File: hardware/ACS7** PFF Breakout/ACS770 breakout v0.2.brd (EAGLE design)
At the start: 54.3 x 21.6 mm, 19 parts

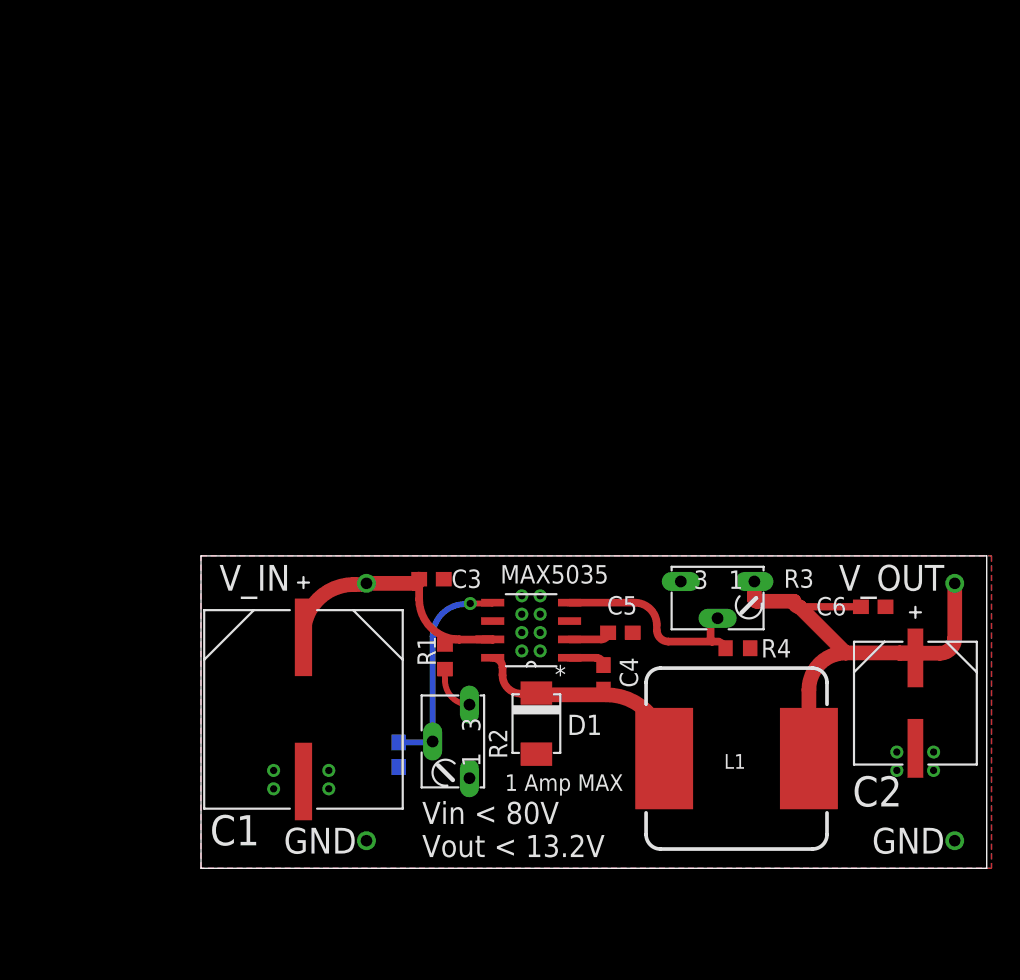
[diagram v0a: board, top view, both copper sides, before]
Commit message: acs7** addition, emonBuck update
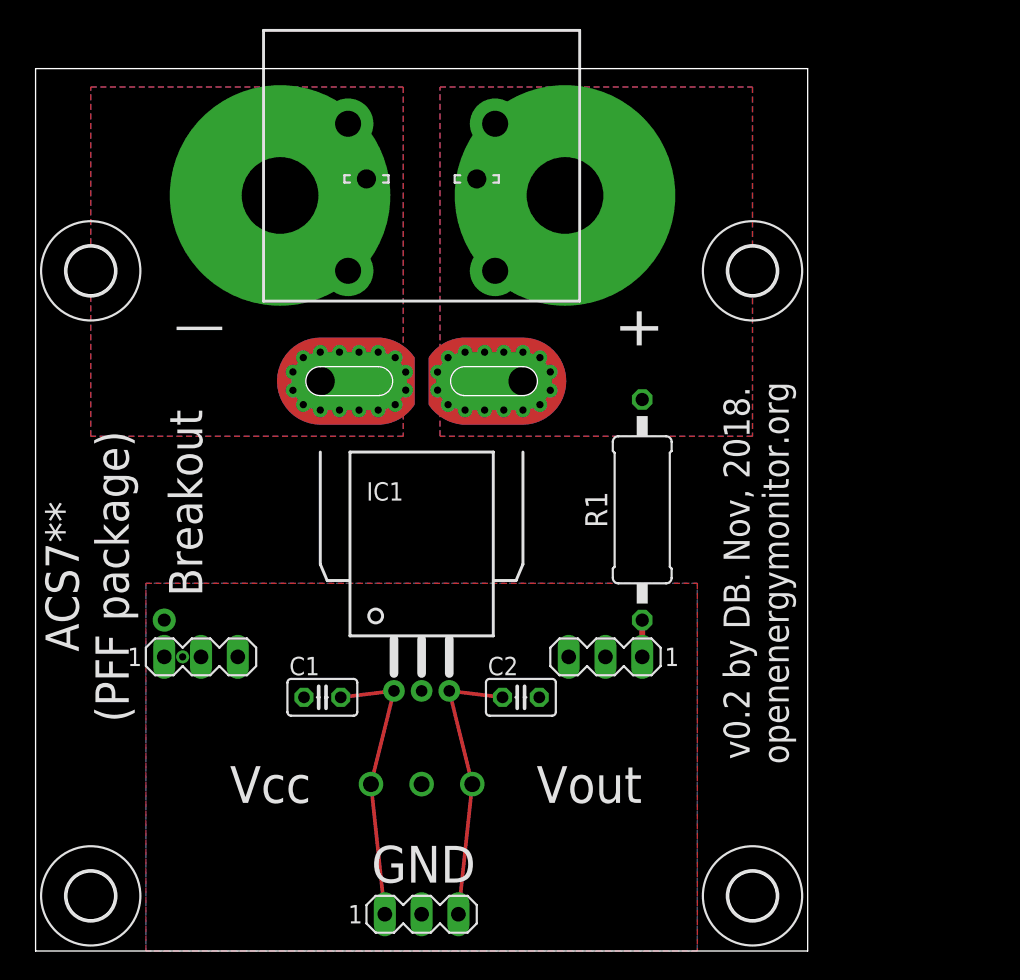
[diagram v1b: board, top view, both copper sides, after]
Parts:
- removed C3, C4, C5, C6, C7: 0.1uF 100V, rcl:C0603
- removed D1: MBRS1100T3G, diodes:SMB_1
- removed L1: SRR1208, inductor-bourns:SSR1208
- removed LOGO1: OSHW_LOGO_6MILX0200-NT, ohw-logo:OSHW_6X200_NOTEXT
- removed MAX5035: MAX5035, MAX5035:21-0111D_SBE-14
- removed R2, R3: 200k, pot:B64W
- removed R4: 10k, rcl@1:R0603
- added IC1: ACS770_PFF, allegro:CB-PFF
- added LSP1, LSP2: LSP13, solpad:LSP13
- added SV1, SV2, SV3: (no value), con-lstb:MA03-1
- added U$5: MOLEX_39970-003, 10.16mm terminal block:2/10,16
- added X1: 1751251, con-phoenix-350:1751251
- C1: value 100uF 80V -> 1nF; device Panasonic-EEE-EEV-EEF-ECQ:CAPAE1350X1400N -> rcl7:C025-025X050
- C2: value 470uF 16V -> 1nF; device Panasonic-EEEFK_EEEFP:CAPAE830X1050N -> rcl7:C025-025X050
- R1: value 700K -> 1M; device rcl@1:R0603 -> rcl:0411/15
- U$1, U$2, U$3, U$4: value TP0.8MM -> (none); device testpad_db:TP0.8 -> holes:3,3
- moved U$4 59.8 mm to (3.81, 3.81)
- moved U$2 47.6 mm to (49.5, 47.0)
- moved U$1 28.8 mm to (3.81, 47.0)
- moved C2 27.3 mm to (33.5, 17.5), turned to 0 degrees
- moved U$3 25.7 mm to (49.5, 3.81)
- moved R1 17.0 mm to (41.9, 30.5), turned to 270 degrees
- moved C1 1.55 mm to (19.8, 17.5), turned to 0 degrees
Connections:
- removed net BST: C4.1, MAX5035.1
- removed net LX: C4.2, D1.C, L1.1, MAX5035.8
- removed net PRE_6.5V: C2.1, C6.1, L1.2, R3.A, U$3.P$1
- removed net VD: C5.1, MAX5035.2
- removed net V_IN_POSTFUSE: C1.1, C3.1, MAX5035.7, R1.2, U$1.P$1
- new net N$4: IC1.IP-, IC1.IP-@10, IC1.IP-@11, IC1.IP-@12, IC1.IP-@13, IC1.IP-@14, IC1.IP-@15, IC1.IP-@16, IC1.IP-@17, IC1.IP-@2, IC1.IP-@3, IC1.IP-@4, IC1.IP-@5, IC1.IP-@6, IC1.IP-@7, IC1.IP-@8, IC1.IP-@9, LSP2.MP, U$5.P$3, U$5.P$4
- new net N$5: IC1.IP+, IC1.IP+@10, IC1.IP+@11, IC1.IP+@12, IC1.IP+@13, IC1.IP+@14, IC1.IP+@15, IC1.IP+@16, IC1.IP+@17, IC1.IP+@2, IC1.IP+@3, IC1.IP+@4, IC1.IP+@5, IC1.IP+@6, IC1.IP+@7, IC1.IP+@8, IC1.IP+@9, LSP1.MP, R1.1, U$5.P$1, U$5.P$2
- net GND: now also C1.1, IC1.2, SV1.2, X1.2; no longer C1.2, C3.2, C5.2, C6.2, C7.2, D1.A, MAX5035.3, MAX5035.6, R2.A, R4.1, U$2.P$1, U$4.P$1
- net N$1: now also C1.2, IC1.1, SV1.1, X1.1; no longer MAX5035.4, R3.S, R4.2
- net N$2: now also R1.2, SV2.1; no longer C7.1, MAX5035.5, R2.S
- net N$3: now also C2.1, IC1.3, SV1.3, X1.3; no longer R1.1, R2.E
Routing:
- net PRE_6.5V: track 34.6 -> 0.00 mm
- net V_IN_POSTFUSE: track 20.3 -> 0.00 mm
- net N$3: track 3.15 -> 19.4 mm
- net LX: track 15.8 -> 0.00 mm
- net N$2: track 14.7 -> 2.54 mm, vias 1 -> 0
- net N$1: track 14.1 -> 19.4 mm
- net VD: track 2.86 -> 0.00 mm
- net BST: track 2.55 -> 0.00 mm
- added copper zone on layer 1, net N$4
- added copper zone on layer 16, net N$4
- added copper zone on layer 1, net N$5
- added copper zone on layer 16, net N$5
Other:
- board size 54.3 x 21.6 mm -> 53.3 x 61 mm
- board text added: "+"
- board text added: "ACS7** (PFF package)"
- board text added: "Breakout"
- board text added: "Vcc"
- board text added: "Vout"
- board text added: "v0.2 by DB. Nov, 2018. openenergymonitor.org"
- board text added: "|"
- board text removed: "1 Amp MAX"
- board text removed: "125kHz"
- board text removed: "Adjustable DC-DC Buck Power Supply November, 2018 by DB OpenEnergyMonitor.org"
- board text removed: "V_IN"
- board text removed: "V_OUT"
- board text removed: "Vin < 80V Vout < 13.2V"
